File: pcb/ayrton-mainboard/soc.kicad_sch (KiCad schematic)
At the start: 1 part, among them U1 STM32MP257FAI3

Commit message: Continued initial system design
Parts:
- removed unit 9 of U1
- removed unit 4 of U1
- removed unit 7 of U1
- removed unit 3 of U1
- removed unit 8 of U1
- added J1: CORTEX_DEBUG_ETM, symbol special-azonenberg:CORTEX_DEBUG_ETM
- added R1: 33, symbol device:R
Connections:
- net TRACED1: now reaches U1.H1 (PF14)
- net TRACED1: now also J1.16 (TRACED1)
- net TRACECLK: now reaches U1.K3 (PF12)
- net TRACECLK: now also J1.12 (TRACECLK)
- net TRACED0: now reaches U1.L4 (PF13)
- net TRACED0: now also J1.14 (TRACED0)
- net TRACED2: now reaches U1.L7 (PF15)
- net TRACED2: now also J1.18 (TRACED2)
- net TRACED3: now reaches U1.L1 (PG5)
- net TRACED3: now also J1.20 (TRACED3)
- net SOC_CLK: now reaches U1.V3 (OSC_IN)
- net GND: now reaches U1.W5 (VREF-)
- net GND: now also J1.11 (GND), J1.13 (GND), J1.15 (GND), J1.17 (GND), J1.19 (GND), J1.3 (GND), J1.5 (GND), J1.9 (GNDdet)
- net SOC_TCK: now reaches U1.AA1 (JTCK)
- net SOC_TCK: now also J1.4 (TCK)
- net SOC_JTRST_N: now reaches U1.AA2 (NJTRST)
- net SOC_TDI: now reaches U1.AB2 (JTDI)
- net SOC_TDI: now also J1.8 (TDI)
- net SOC_BOOT1: now reaches U1.R3 (BOOT1)
- net SOC_BOOT0: now reaches U1.R4 (BOOT0)
- net SOC_BOOT3: now reaches U1.T1 (BOOT3)
- net SOC_BOOT2: now reaches U1.T2 (BOOT2)
- net at U1.W1 (JTDO): now also R1.2
- net SOC_TMS: now reaches U1.Y1 (JTMS)
- net SOC_TMS: now also J1.2 (TMS)
- new net 3V3: J1.1 (VCC)
- new net SOC_TDO: J1.6 (TDO), R1.1
- no-connect marks 0 -> 2
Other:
- added sheet SoC unused peripherals (soc-unused.kicad_sch)
- sheet SoC RAM ports: added 1V1, 1V8, GND; removed none
- sheet SoC power ports: added 0V8, 0V82, 1V1, 1V8, 3V3, GND; removed none
- note added: "TODO: 32 kHz clock for RTC"
- moved on the sheet: U1A, U1B, U1K, U1L, U1M, U1N, U1O, U1P, U1Q, U1R, U1S, U1T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

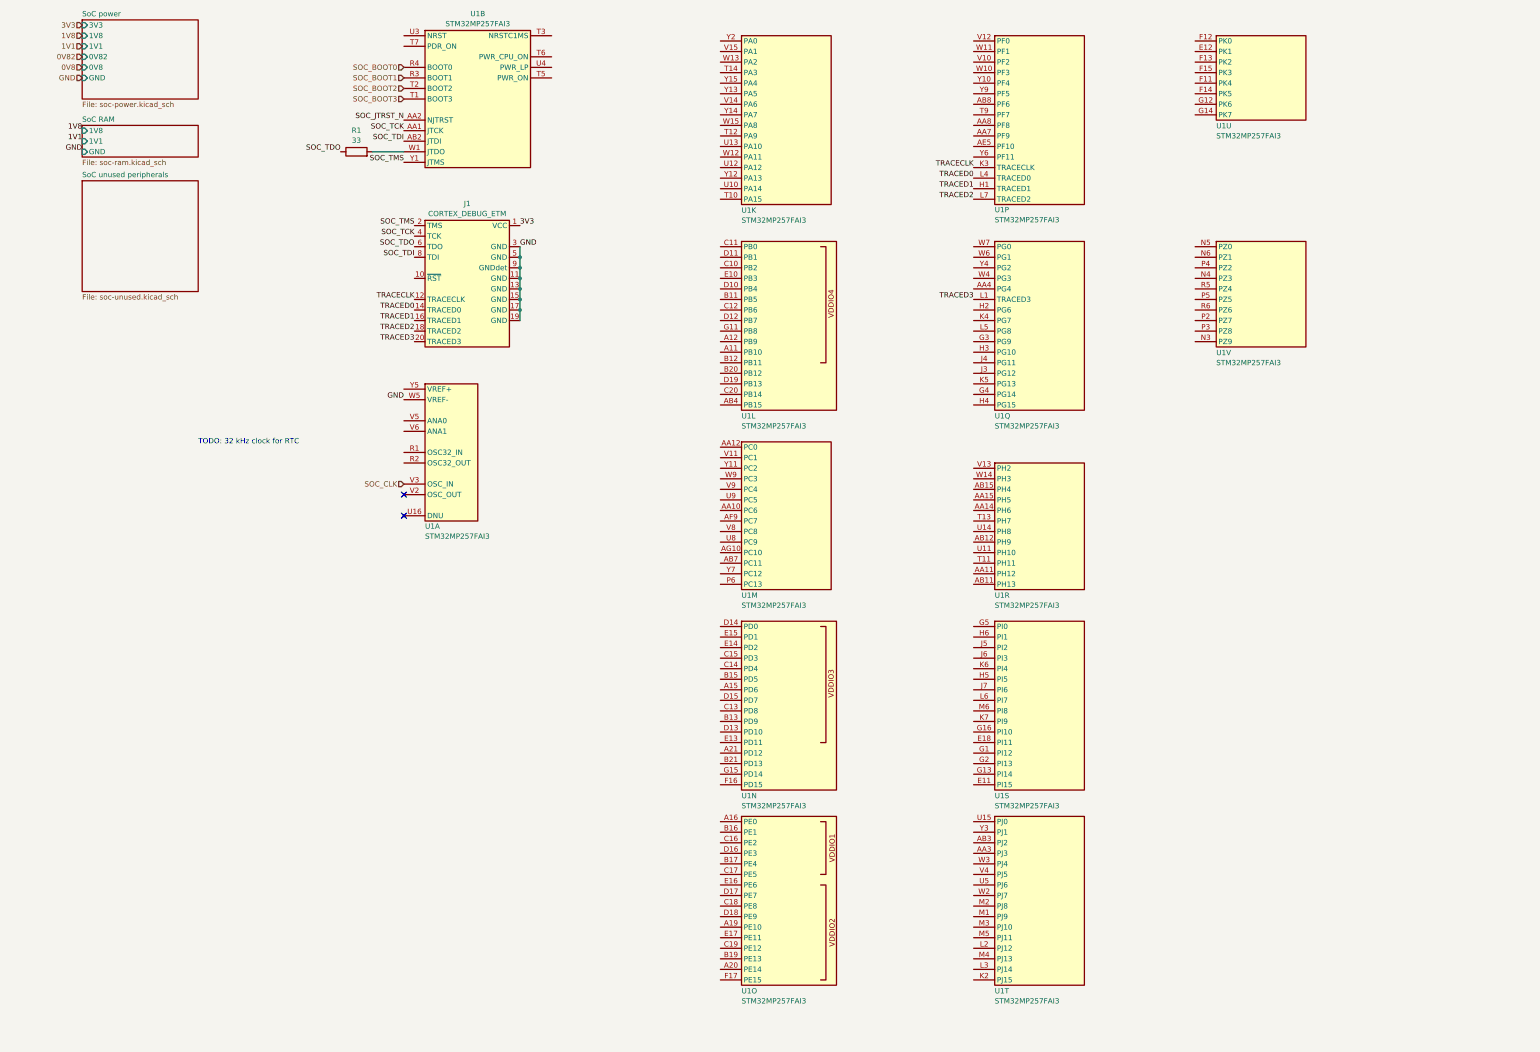
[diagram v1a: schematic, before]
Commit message: Continued initial schematic, working on LPDDR4
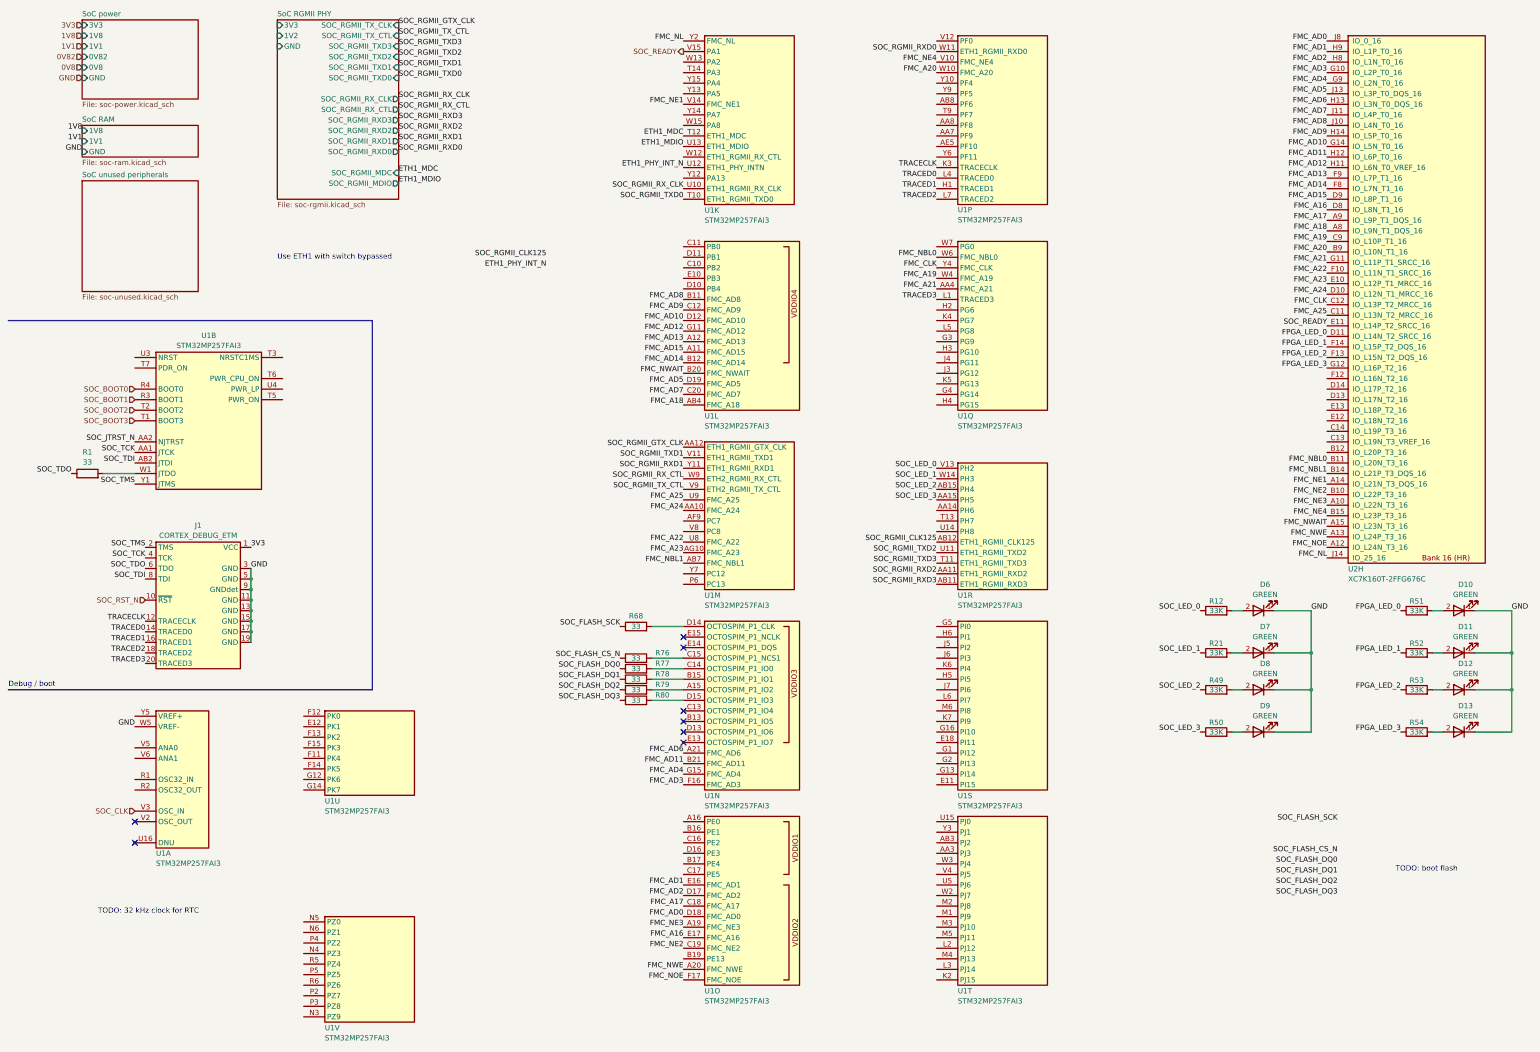
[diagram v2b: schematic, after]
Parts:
- added D10, D11, D12, D13, D6, D7, D8, D9: GREEN, azonenberg_pcb:EIA_0402_LED, symbol device:LED
- added R12, R21, R49, R50, R51, R52, R53, R54: 33K, azonenberg_pcb:EIA_0402_RES_NOSILK, symbol device:R
- added R68, R76, R77, R78, R79, R80: 33, symbol device:R
- added U2: XC7K160T-2FFG676C, symbol xilinx-azonenberg:XC7KxT-FFG676
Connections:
- net GND: now also D10.1 (K), D11.1 (K), D12.1 (K), D13.1 (K), D6.1 (K), D7.1 (K), D8.1 (K), D9.1 (K)
- net at U1.A15 (PD6): now also R79.2
- net FMC_AD6: now reaches U1.A21 (PD12)
- net FMC_AD6: now also U2.H13 (IO_L3N_T0_DQS_16)
- net at U1.B15 (PD5): now also R78.2
- net FMC_AD11: now reaches U1.B21 (PD13)
- net FMC_AD11: now also U2.H12 (IO_L6P_T0_16)
- net at U1.C14 (PD4): now also R77.2
- net at U1.C15 (PD3): now also R76.2
- net at U1.D14 (PD0): now also R68.2
- net at U1.D15 (PD7): now also R80.2
- net FMC_AD3: now reaches U1.F16 (PD15)
- net FMC_AD3: now also U2.G10 (IO_L2P_T0_16)
- net FMC_AD4: now reaches U1.G15 (PD14)
- net FMC_AD4: now also U2.G9 (IO_L2N_T0_16)
- net FMC_AD15: now reaches U1.A11 (PB10)
- net FMC_AD15: now also U2.D9 (IO_L8P_T1_16)
- net FMC_AD13: now reaches U1.A12 (PB9)
- net FMC_AD13: now also U2.F9 (IO_L7P_T1_16)
- net FMC_A18: now reaches U1.AB4 (PB15)
- net FMC_A18: now also U2.A8 (IO_L9N_T1_DQS_16)
- net FMC_AD8: now reaches U1.B11 (PB5)
- net FMC_AD8: now also U2.J10 (IO_L4N_T0_16)
- net FMC_AD14: now reaches U1.B12 (PB11)
- net FMC_AD14: now also U2.F8 (IO_L7N_T1_16)
- net FMC_NWAIT: now reaches U1.B20 (PB12)
- net FMC_NWAIT: now also U2.A15 (IO_L23N_T3_16)
- net FMC_AD9: now reaches U1.C12 (PB6)
- net FMC_AD9: now also U2.H14 (IO_L5P_T0_16)
- net FMC_AD7: now reaches U1.C20 (PB14)
- net FMC_AD7: now also U2.J11 (IO_L4P_T0_16)
- net FMC_AD10: now reaches U1.D12 (PB7)
- net FMC_AD10: now also U2.G14 (IO_L5N_T0_16)
- net FMC_AD5: now reaches U1.D19 (PB13)
- net FMC_AD5: now also U2.J13 (IO_L3P_T0_DQS_16)
- net FMC_AD12: now reaches U1.G11 (PB8)
- net FMC_AD12: now also U2.H11 (IO_L6N_T0_VREF_16)
- net SOC_RGMII_TXD0: now reaches U1.T10 (PA15)
- net ETH1_MDC: now reaches U1.T12 (PA9)
- net SOC_RGMII_RX_CLK: now reaches U1.U10 (PA14)
- net ETH1_PHY_INT_N: now reaches U1.U12 (PA12)
- net ETH1_MDIO: now reaches U1.U13 (PA10)
- net FMC_NE1: now reaches U1.V14 (PA6)
- net FMC_NE1: now also U2.A14 (IO_L21N_T3_DQS_16)
- net SOC_READY: now reaches U1.V15 (PA1)
- net SOC_READY: now also U2.E11 (IO_L14P_T2_SRCC_16)
- net FMC_NL: now reaches U1.Y2 (PA0)
- net FMC_NL: now also U2.J14 (IO_25_16)
- net SOC_RGMII_RXD2: now reaches U1.AA11 (PH12)
- net SOC_LED_3: now reaches U1.AA15 (PH5)
- net SOC_LED_3: now also R50.1
- net SOC_RGMII_RXD3: now reaches U1.AB11 (PH13)
- net SOC_RGMII_CLK125: now reaches U1.AB12 (PH9)
- net SOC_LED_2: now reaches U1.AB15 (PH4)
- net SOC_LED_2: now also R49.1
- net SOC_RGMII_TXD3: now reaches U1.T11 (PH11)
- net SOC_RGMII_TXD2: now reaches U1.U11 (PH10)
- net SOC_LED_0: now reaches U1.V13 (PH2)
- net SOC_LED_0: now also R12.1
- net SOC_LED_1: now reaches U1.W14 (PH3)
- net SOC_LED_1: now also R21.1
- net SOC_RST_N: now reaches J1.10 (~{RST})
- net FMC_NE4: now reaches U1.V10 (PF2)
- net FMC_NE4: now also U2.B15 (IO_L23P_T3_16)
- net FMC_A20: now reaches U1.W10 (PF3)
- net FMC_A20: now also U2.B9 (IO_L10N_T1_16)
- net SOC_RGMII_RXD0: now reaches U1.W11 (PF1)
- net FMC_NE3: now reaches U1.A19 (PE10)
- net FMC_NE3: now also U2.A10 (IO_L22N_T3_16)
- net FMC_NWE: now reaches U1.A20 (PE14)
- net FMC_NWE: now also U2.A13 (IO_L24P_T3_16)
- net FMC_A17: now reaches U1.C18 (PE8)
- net FMC_A17: now also U2.A9 (IO_L9P_T1_DQS_16)
- net FMC_NE2: now reaches U1.C19 (PE12)
- net FMC_NE2: now also U2.B10 (IO_L22P_T3_16)
- net FMC_AD2: now reaches U1.D17 (PE7)
- net FMC_AD2: now also U2.H8 (IO_L1N_T0_16)
- net FMC_AD0: now reaches U1.D18 (PE9)
- net FMC_AD0: now also U2.J8 (IO_0_16)
- net FMC_AD1: now reaches U1.E16 (PE6)
- net FMC_AD1: now also U2.H9 (IO_L1P_T0_16)
- net FMC_A16: now reaches U1.E17 (PE11)
- net FMC_A16: now also U2.D8 (IO_L8N_T1_16)
- net FMC_NOE: now reaches U1.F17 (PE15)
- net FMC_NOE: now also U2.A12 (IO_L24N_T3_16)
- net FMC_A21: now reaches U1.AA4 (PG4)
- net FMC_A21: now also U2.G11 (IO_L11P_T1_SRCC_16)
- net FMC_A19: now reaches U1.W4 (PG3)
- net FMC_A19: now also U2.C9 (IO_L10P_T1_16)
- net FMC_NBL0: now reaches U1.W6 (PG1)
- net FMC_NBL0: now also U2.B11 (IO_L20N_T3_16)
- net FMC_CLK: now reaches U1.Y4 (PG2)
- net FMC_CLK: now also U2.C12 (IO_L13P_T2_MRCC_16)
- net FMC_A24: now reaches U1.AA10 (PC6)
- net FMC_A24: now also U2.D10 (IO_L12N_T1_MRCC_16)
- net SOC_RGMII_GTX_CLK: now reaches U1.AA12 (PC0)
- net FMC_NBL1: now reaches U1.AB7 (PC11)
- net FMC_NBL1: now also U2.B14 (IO_L21P_T3_DQS_16)
- net FMC_A23: now reaches U1.AG10 (PC10)
- net FMC_A23: now also U2.E10 (IO_L12P_T1_MRCC_16)
- net FMC_A22: now reaches U1.U8 (PC9)
- net FMC_A22: now also U2.F10 (IO_L11N_T1_SRCC_16)
- net FMC_A25: now reaches U1.U9 (PC5)
- net FMC_A25: now also U2.C11 (IO_L13N_T2_MRCC_16)
- net SOC_RGMII_TXD1: now reaches U1.V11 (PC1)
- net SOC_RGMII_TX_CTL: now reaches U1.V9 (PC4)
- net SOC_RGMII_RX_CTL: now reaches U1.W9 (PC3)
- net SOC_RGMII_RXD1: now reaches U1.Y11 (PC2)
- new net: D10.2 (A), R51.2
- new net: D12.2 (A), R53.2
- new net: D9.2 (A), R50.2
- new net: D6.2 (A), R12.2
- new net: D11.2 (A), R52.2
- new net: D8.2 (A), R49.2
- new net: D7.2 (A), R21.2
- new net: D13.2 (A), R54.2
- new net FPGA_LED_0: R51.1, U2.D11 (IO_L14N_T2_SRCC_16)
- new net FPGA_LED_1: R52.1, U2.F14 (IO_L15P_T2_DQS_16)
- new net FPGA_LED_2: R53.1, U2.F13 (IO_L15N_T2_DQS_16)
- new net FPGA_LED_3: R54.1, U2.G12 (IO_L16P_T2_16)
- new net SOC_FLASH_CS_N: R76.1
- new net SOC_FLASH_DQ0: R77.1
- new net SOC_FLASH_DQ1: R78.1
- new net SOC_FLASH_DQ2: R79.1
- new net SOC_FLASH_DQ3: R80.1
- new net SOC_FLASH_SCK: R68.1
- no-connect marks 2 -> 8
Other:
- added sheet SoC RGMII PHY (soc-rgmii.kicad_sch)
- note added: "Debug / boot"
- note added: "TODO: boot flash"
- note added: "Use ETH1 with switch bypassed"
- moved on the sheet: J1, R1, U1A, U1B, U1K, U1L, U1M, U1N, U1O, U1P, U1Q, U1R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
